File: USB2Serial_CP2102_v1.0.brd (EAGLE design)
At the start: 23.3 x 25.5 mm, 23 parts, among them CN1 UART, CN2 47346-0001, IC1 AMS1117-3.3, U3 CP2102

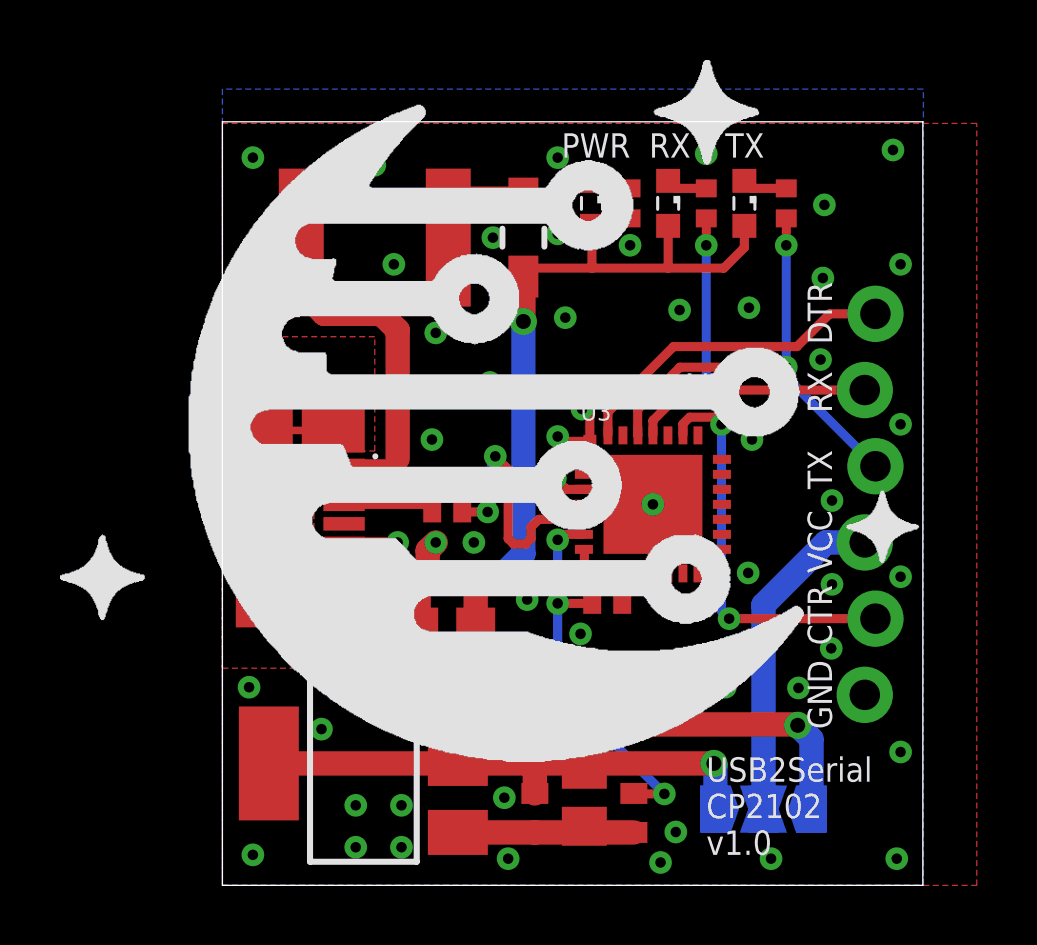
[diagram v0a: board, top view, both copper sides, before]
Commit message: Moved some traced around
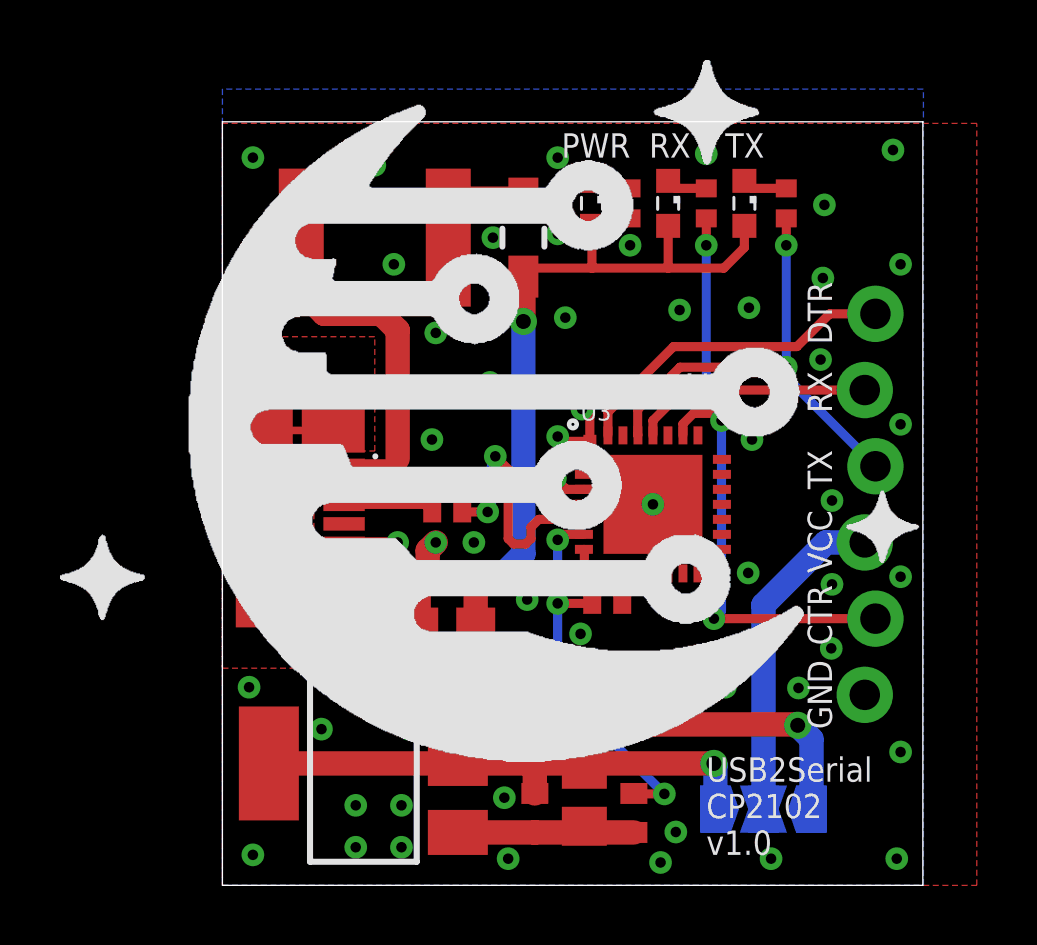
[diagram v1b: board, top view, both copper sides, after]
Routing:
- net UART_CTS: track 13.3 -> 14.0 mm
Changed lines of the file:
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@@
 CP2102
 v1.0</text>
+<circle x="11.684" y="15.367" radius="0.127" width="0.1524" layer="21"/>
 </plain>
 <attributes>
@@
 <via x="17.526" y="10.414" extent="1-16" drill="0.35"/>
 <via x="17.653" y="14.859" extent="1-16" drill="0.35"/>
-<via x="15.621" y="9.144" extent="1-16" drill="0.35"/>
+<via x="15.24" y="9.271" extent="1-16" drill="0.35"/>
 <via x="22.606" y="10.287" extent="1-16" drill="0.35"/>
 <via x="20.32" y="10.033" extent="1-16" drill="0.35"/>
@@
 <contactref element="CN1" pad="5"/>
 <contactref element="U3" pad="23"/>
-<wire x1="21.7678" y1="8.89" x2="16.891" y2="8.89" width="0.3048" layer="1"/>
-<via x="16.891" y="8.89" extent="1-16" drill="0.35"/>
-<wire x1="16.891" y1="8.89" x2="16.637" y2="9.144" width="0.3048" layer="16"/>
-<wire x1="16.637" y1="9.144" x2="16.637" y2="15.367" width="0.3048" layer="16"/>
-<via x="16.637" y="15.367" extent="1-16" drill="0.35"/>
-<wire x1="16.637" y1="15.367" x2="16.637" y2="15.37445" width="0.3048" layer="1"/>
-<wire x1="16.637" y1="15.37445" x2="16.40665" y2="15.6048" width="0.3048" layer="1"/>
-<wire x1="16.40665" y1="15.6048" x2="15.57475" y2="15.6048" width="0.3048" layer="1"/>
+<wire x1="21.7678" y1="8.89" x2="16.383" y2="8.89" width="0.3048" layer="1"/>
+<via x="16.383" y="8.89" extent="1-16" drill="0.35"/>
+<wire x1="16.383" y1="8.89" x2="16.637" y2="9.144" width="0.3048" layer="16"/>
+<wire x1="16.637" y1="9.144" x2="16.637" y2="15.494" width="0.3048" layer="16"/>
+<via x="16.637" y="15.494" extent="1-16" drill="0.35"/>
+<wire x1="16.637" y1="15.494" x2="16.637" y2="15.50145" width="0.3048" layer="1"/>
+<wire x1="16.637" y1="15.50145" x2="16.40665" y2="15.7318" width="0.3048" layer="1"/>
+<wire x1="16.40665" y1="15.7318" x2="15.70175" y2="15.7318" width="0.3048" layer="1"/>
 <wire x1="15.351" y1="15" x2="15.351" y2="15.38105" width="0.3048" layer="1"/>
-<wire x1="15.351" y1="15.38105" x2="15.57475" y2="15.6048" width="0.3048" layer="1"/>
+<wire x1="15.351" y1="15.38105" x2="15.70175" y2="15.7318" width="0.3048" layer="1"/>
 </signal>
 <signal name="VCC">
